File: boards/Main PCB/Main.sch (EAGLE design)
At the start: 120 parts, among them CN1 MINIB, CN2 MINIB, IC1 FT232RL, IC2 FT232RL, IC4 OKR-T_3-W12-C, J1 3_PIN_JST-XH, J2 2_PIN_JST-XH, J3 5_PIN_JST-XH, Q4 BSS138, Q5 BSS138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

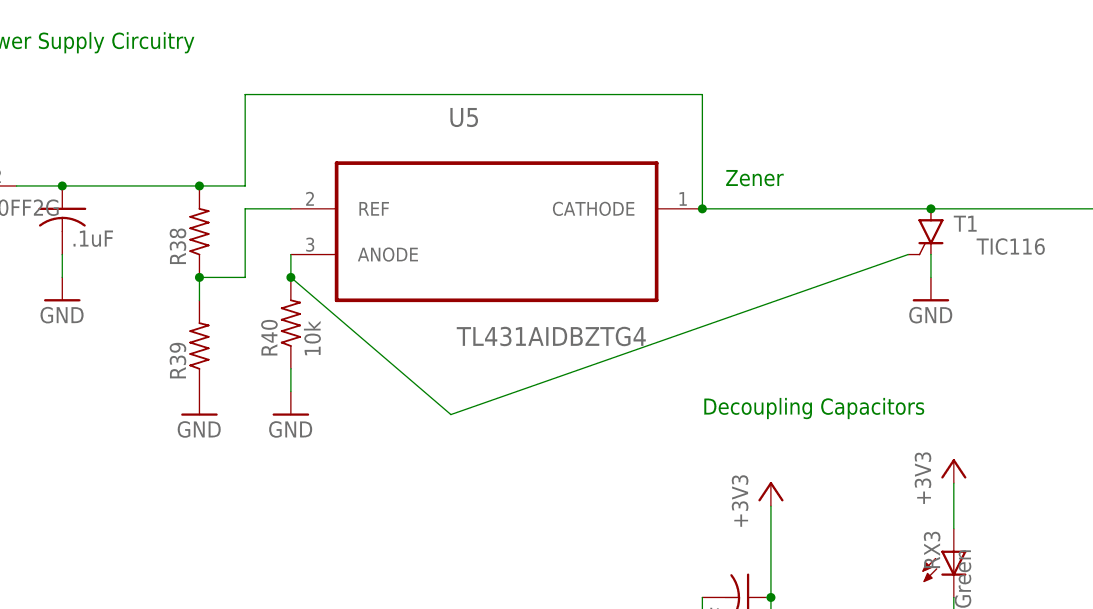
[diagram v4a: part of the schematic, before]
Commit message: Routed crowbar circuit
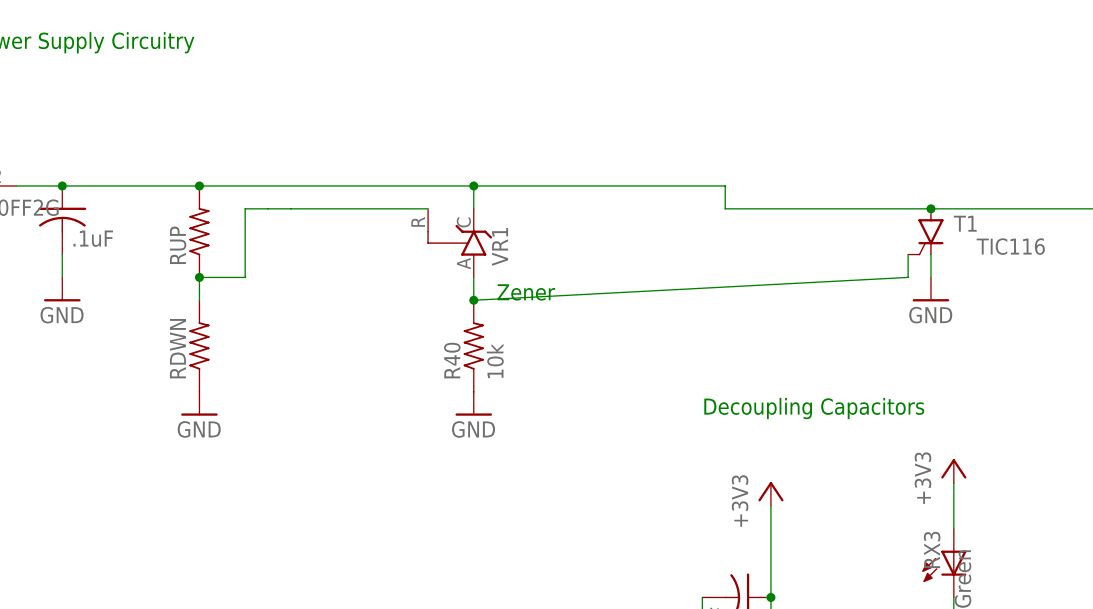
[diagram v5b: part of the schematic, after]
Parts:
- removed U5: TL431AIDBZTG4, main_library:TL431AIDBZTG4
- added VR1: (no value), v-reg:TL431CLP
- renumbered R38 to RUP, R39 to RDWN
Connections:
- removed net N$30: R40.2, T1.G, U5.ANODE
- new net N$24: R40.2, T1.G, VR1.A
- net +5V: now also VR1.C; no longer U5.CATHODE
- net N$25: now also VR1.R; no longer U5.REF
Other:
- moved on the sheet: R40
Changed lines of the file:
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@@
 <part name="C33" library="rcl" library_urn="urn:adsk.eagle:library:334" deviceset="C-US" device="C0805" package3d_urn="urn:adsk.eagle:package:23617/2" value=".1uF"/>
 <part name="GND48" library="supply1" library_urn="urn:adsk.eagle:library:371" deviceset="GND" device=""/>
-<part name="R38" library="resistor" library_urn="urn:adsk.eagle:library:348" deviceset="R-US_" device="R0805" package3d_urn="urn:adsk.eagle:package:26059/1"/>
-<part name="R39" library="resistor" library_urn="urn:adsk.eagle:library:348" deviceset="R-US_" device="R0805" package3d_urn="urn:adsk.eagle:package:26059/1"/>
+<part name="RUP" library="resistor" library_urn="urn:adsk.eagle:library:348" deviceset="R-US_" device="R0805" package3d_urn="urn:adsk.eagle:package:26059/1"/>
+<part name="RDWN" library="resistor" library_urn="urn:adsk.eagle:library:348" deviceset="R-US_" device="R0805" package3d_urn="urn:adsk.eagle:package:26059/1"/>
 <part name="GND49" library="supply1" library_urn="urn:adsk.eagle:library:371" deviceset="GND" device=""/>
-<part name="U5" library="main_library" deviceset="TL431AIDBZTG4" device=""/>
 <part name="GND50" library="supply1" library_urn="urn:adsk.eagle:library:371" deviceset="GND" device=""/>
 <part name="R40" library="resistor" library_urn="urn:adsk.eagle:library:348" deviceset="R-US_" device="R0805" package3d_urn="urn:adsk.eagle:package:26059/1" value="10k"/>
 <part name="T1" library="triac" library_urn="urn:adsk.eagle:library:403" deviceset="TIC116" device="" package3d_urn="urn:adsk.eagle:package:30140/2"/>
 <part name="GND51" library="supply1" library_urn="urn:adsk.eagle:library:371" deviceset="GND" device=""/>
+<part name="VR1" library="v-reg" library_urn="urn:adsk.eagle:library:409" deviceset="TL431CLP" device="" package3d_urn="urn:adsk.eagle:package:30363/1"/>
 </parts>
 <sheets>
@@
 <text x="122.682" y="110.744" size="1.778" layer="95">10K</text>
 <text x="112.522" y="128.524" size="1.778" layer="95">10K</text>
-<text x="406.4" y="383.54" size="1.778" layer="91">Zener</text>
+<text x="381" y="370.84" size="1.778" layer="91">Zener</text>
 </plain>
 <instances>
@@
 <attribute name="VALUE" x="474.98" y="228.6" size="1.778" layer="96"/>
 </instance>
-<instance part="R38" gate="G$1" x="347.98" y="378.46" smashed="yes" rot="R90">
+<instance part="RUP" gate="G$1" x="347.98" y="378.46" smashed="yes" rot="R90">
 <attribute name="NAME" x="346.4814" y="374.65" size="1.778" layer="95" rot="R90"/>
 <attribute name="VALUE" x="351.282" y="374.65" size="1.778" layer="96" rot="R90"/>
 </instance>
-<instance part="R39" gate="G$1" x="347.98" y="365.76" smashed="yes" rot="R90">
+<instance part="RDWN" gate="G$1" x="347.98" y="365.76" smashed="yes" rot="R90">
 <attribute name="NAME" x="346.4814" y="361.95" size="1.778" layer="95" rot="R90"/>
 <attribute name="VALUE" x="351.282" y="361.95" size="1.778" layer="96" rot="R90"/>
@@
 <attribute name="VALUE" x="345.44" y="355.6" size="1.778" layer="96"/>
 </instance>
-<instance part="U5" gate="A" x="381" y="381" smashed="yes">
-<attribute name="NAME" x="375.636409375" y="390.12573125" size="2.08443125" layer="95" ratio="10" rot="SR0"/>
-<attribute name="VALUE" x="376.57783125" y="365.7765" size="2.084009375" layer="96" ratio="10" rot="SR0"/>
-</instance>
-<instance part="GND50" gate="1" x="358.14" y="358.14" smashed="yes">
-<attribute name="VALUE" x="355.6" y="355.6" size="1.778" layer="96"/>
-</instance>
-<instance part="R40" gate="G$1" x="358.14" y="368.3" smashed="yes" rot="R90">
-<attribute name="NAME" x="356.6414" y="364.49" size="1.778" layer="95" rot="R90"/>
-<attribute name="VALUE" x="361.442" y="364.49" size="1.778" layer="96" rot="R90"/>
+<instance part="GND50" gate="1" x="378.46" y="358.14" smashed="yes">
+<attribute name="VALUE" x="375.92" y="355.6" size="1.778" layer="96"/>
+</instance>
+<instance part="R40" gate="G$1" x="378.46" y="365.76" smashed="yes" rot="R90">
+<attribute name="NAME" x="376.9614" y="361.95" size="1.778" layer="95" rot="R90"/>
+<attribute name="VALUE" x="381.762" y="361.95" size="1.778" layer="96" rot="R90"/>
 </instance>
 <instance part="T1" gate="1" x="429.26" y="378.46" smashed="yes">
@@
 <instance part="GND51" gate="1" x="429.26" y="370.84" smashed="yes">
 <attribute name="VALUE" x="426.72" y="368.3" size="1.778" layer="96"/>
+</instance>
+<instance part="VR1" gate="G$1" x="378.46" y="378.46" smashed="yes" rot="R90">
+<attribute name="NAME" x="382.27" y="374.65" size="1.778" layer="95" rot="R90"/>
+<attribute name="VALUE" x="384.175" y="374.65" size="1.778" layer="96" rot="R90"/>
 </instance>
 </instances>
@@
 </segment>
 <segment>
-<pinref part="R39" gate="G$1" pin="1"/>
+<pinref part="RDWN" gate="G$1" pin="1"/>
 <pinref part="GND49" gate="1" pin="GND"/>
-</segment>
-<segment>
-<pinref part="R40" gate="G$1" pin="1"/>
-<pinref part="GND50" gate="1" pin="GND"/>
-<wire x1="358.14" y1="363.22" x2="358.14" y2="360.68" width="0.1524" layer="91"/>
 </segment>
 <segment>
@@
 <pinref part="GND51" gate="1" pin="GND"/>
 <wire x1="429.26" y1="375.92" x2="429.26" y2="373.38" width="0.1524" layer="91"/>
+</segment>
+<segment>
+<pinref part="R40" gate="G$1" pin="1"/>
+<pinref part="GND50" gate="1" pin="GND"/>
 </segment>
 </net>
@@
 <pinref part="P+1" gate="1" pin="+5V"/>
 <wire x1="472.44" y1="388.62" x2="472.44" y2="381" width="0.1524" layer="91"/>
+<pinref part="T1" gate="1" pin="A"/>
+<wire x1="406.4" y1="381" x2="429.26" y2="381" width="0.1524" layer="91"/>
+<wire x1="429.26" y1="381" x2="472.44" y2="381" width="0.1524" layer="91"/>
+<junction x="429.26" y="381"/>
+<junction x="472.44" y="381"/>
+<pinref part="VR1" gate="G$1" pin="C"/>
+<pinref part="RUP" gate="G$1" pin="2"/>
 <pinref part="C8" gate="G$1" pin="1"/>
 <pinref part="R33" gate="G$1" pin="2"/>
 <wire x1="327.66" y1="383.54" x2="332.74" y2="383.54" width="0.1524" layer="91"/>
-<pinref part="R38" gate="G$1" pin="2"/>
+<junction x="332.74" y="383.54"/>
 <wire x1="332.74" y1="383.54" x2="347.98" y2="383.54" width="0.1524" layer="91"/>
-<junction x="332.74" y="383.54"/>
-<wire x1="347.98" y1="383.54" x2="353.06" y2="383.54" width="0.1524" layer="91"/>
-<wire x1="353.06" y1="383.54" x2="353.06" y2="393.7" width="0.1524" layer="91"/>
 <junction x="347.98" y="383.54"/>
-<pinref part="U5" gate="A" pin="CATHODE"/>
-<wire x1="353.06" y1="393.7" x2="403.86" y2="393.7" width="0.1524" layer="91"/>
-<wire x1="403.86" y1="393.7" x2="403.86" y2="381" width="0.1524" layer="91"/>
-<pinref part="T1" gate="1" pin="A"/>
-<wire x1="403.86" y1="381" x2="429.26" y2="381" width="0.1524" layer="91"/>
-<junction x="403.86" y="381"/>
-<wire x1="429.26" y1="381" x2="472.44" y2="381" width="0.1524" layer="91"/>
-<junction x="429.26" y="381"/>
-<junction x="472.44" y="381"/>
+<wire x1="347.98" y1="383.54" x2="378.46" y2="383.54" width="0.1524" layer="91"/>
+<wire x1="378.46" y1="383.54" x2="378.46" y2="381" width="0.1524" layer="91"/>
+<wire x1="378.46" y1="383.54" x2="406.4" y2="383.54" width="0.1524" layer="91"/>
+<wire x1="406.4" y1="383.54" x2="406.4" y2="381" width="0.1524" layer="91"/>
+<junction x="378.46" y="383.54"/>
 </segment>
 </net>
@@
 <net name="N$25" class="0">
 <segment>
-<pinref part="R38" gate="G$1" pin="1"/>
-<pinref part="R39" gate="G$1" pin="2"/>
+<pinref part="RUP" gate="G$1" pin="1"/>
+<pinref part="RDWN" gate="G$1" pin="2"/>
 <wire x1="347.98" y1="373.38" x2="347.98" y2="370.84" width="0.1524" layer="91"/>
 <wire x1="347.98" y1="373.38" x2="353.06" y2="373.38" width="0.1524" layer="91"/>
 <wire x1="353.06" y1="373.38" x2="353.06" y2="381" width="0.1524" layer="91"/>
 <junction x="347.98" y="373.38"/>
-<pinref part="U5" gate="A" pin="REF"/>
-<wire x1="353.06" y1="381" x2="358.14" y2="381" width="0.1524" layer="91"/>
-</segment>
-</net>
-<net name="N$30" class="0">
-<segment>
-<pinref part="U5" gate="A" pin="ANODE"/>
+<wire x1="353.06" y1="381" x2="355.6" y2="381" width="0.1524" layer="91"/>
+<pinref part="VR1" gate="G$1" pin="R"/>
+<wire x1="355.6" y1="381" x2="358.14" y2="381" width="0.1524" layer="91"/>
+<wire x1="373.38" y1="381" x2="358.14" y2="381" width="0.1524" layer="91"/>
+</segment>
+</net>
+<net name="N$24" class="0">
+<segment>
+<pinref part="VR1" gate="G$1" pin="A"/>
 <pinref part="R40" gate="G$1" pin="2"/>
-<wire x1="358.14" y1="375.92" x2="358.14" y2="373.38" width="0.1524" layer="91"/>
+<wire x1="378.46" y1="373.38" x2="378.46" y2="370.84" width="0.1524" layer="91"/>
 <pinref part="T1" gate="1" pin="G"/>
-<wire x1="358.14" y1="373.38" x2="375.92" y2="358.14" width="0.1524" layer="91"/>
-<wire x1="375.92" y1="358.14" x2="426.72" y2="375.92" width="0.1524" layer="91"/>
-<junction x="358.14" y="373.38"/>
-</segment>
-</net>
+<wire x1="378.46" y1="370.84" x2="426.72" y2="373.38" width="0.1524" layer="91"/>
+<wire x1="426.72" y1="373.38" x2="426.72" y2="375.92" width="0.1524" layer="91"/>
+<junction x="378.46" y="370.84"/>
+</segment>
+</net>

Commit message: Updating with latest PCB submission
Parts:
- removed U$3: BNO055, microbuilder:BNO055
- added U$9: (no value), main_library:MICROBUILDER_BNO055
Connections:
- net +3V3: now also U$9.NBOOT_LOAD_PIN, U$9.VDD, U$9.VDDIO; no longer U$3.NBOOT_LOAD_PIN, U$3.VDD, U$3.VDDIO
- net CAP: now also U$9.CAP; no longer U$3.CAP
- net GND: now also U$9.COM2(GND), U$9.GND@1, U$9.GND@2, U$9.PIN10(GND), U$9.PIN15(GND), U$9.PIN16(GND); no longer U$3.COM2(GND), U$3.GND@1, U$3.GND@2, U$3.PIN10(GND), U$3.PIN15(GND), U$3.PIN16(GND)
- net I2CADDR_3V: now also U$9.COM3/I2C_ADDR; no longer U$3.COM3/I2C_ADDR
- net INT_3V: now also U$9.INT; no longer U$3.INT
- net N$1: now also U$9.XIN32; no longer U$3.XIN32
- net N$10: now also U$9.XOUT32; no longer U$3.XOUT32
- net NRESET_3V: now also U$9.NRESET; no longer U$3.NRESET
- net PS0_3V: now also U$9.PS0; no longer U$3.PS0
- net PS1_3V: now also U$9.PS1; no longer U$3.PS1
- net SCL_3V: now also U$9.COM1/SCL/RX; no longer U$3.COM1/SCL/RX
- net SDA_3V: now also U$9.COM0/SDA/TX; no longer U$3.COM0/SDA/TX
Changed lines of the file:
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@@
 <?xml version="1.0" encoding="utf-8"?>
 <!DOCTYPE eagle SYSTEM "eagle.dtd">
-<eagle version="9.3.1">
+<eagle version="9.3.0">
 <drawing>
 <settings>
@@
 <part name="GND6" library="supply1" library_urn="urn:adsk.eagle:library:371" deviceset="GND" device=""/>
 <part name="R1" library="adafruit" deviceset="R-US_" device="R0805" value="10"/>
-<part name="U$3" library="microbuilder" deviceset="BNO055" device="" value="BNO055"/>
 <part name="R4" library="microbuilder" deviceset="RESISTOR" device="0805_NOOUTLINE" value="10K">
 <attribute name="10K" value=""/>
@@
 <part name="GND51" library="supply1" library_urn="urn:adsk.eagle:library:371" deviceset="GND" device=""/>
 <part name="VR1" library="v-reg" library_urn="urn:adsk.eagle:library:409" deviceset="TL431CLP" device="" package3d_urn="urn:adsk.eagle:package:30363/1"/>
+<part name="U$9" library="main_library" deviceset="MICROBUILDER_BNO055" device=""/>
 </parts>
 <sheets>
@@
 <attribute name="VALUE" x="307.34" y="353.06" size="1.778" layer="96"/>
 </instance>
-<instance part="U$3" gate="G$1" x="71.12" y="121.92" smashed="yes">
-<attribute name="VALUE" x="53.34" y="91.44" size="1.27" layer="96"/>
-</instance>
 <instance part="R4" gate="G$1" x="114.3" y="116.84" smashed="yes">
 <attribute name="VALUE" x="114.3" y="116.84" size="1.016" layer="96" font="vector" ratio="15" align="center"/>
@@
 <attribute name="NAME" x="382.27" y="374.65" size="1.778" layer="95" rot="R90"/>
 <attribute name="VALUE" x="384.175" y="374.65" size="1.778" layer="96" rot="R90"/>
+</instance>
+<instance part="U$9" gate="G$1" x="71.12" y="121.92" smashed="yes">
+<attribute name="NAME" x="53.34" y="148.59" size="1.27" layer="95"/>
+<attribute name="VALUE" x="53.34" y="91.44" size="1.27" layer="96"/>
 </instance>
 </instances>
@@
 </segment>
 <segment>
-<pinref part="U$3" gate="G$1" pin="NBOOT_LOAD_PIN"/>
 <pinref part="U$15" gate="G$1" pin="3.3V"/>
 <wire x1="91.44" y1="109.22" x2="93.98" y2="109.22" width="0.1524" layer="91"/>
-</segment>
-<segment>
-<pinref part="U$3" gate="G$1" pin="VDDIO"/>
+<pinref part="U$9" gate="G$1" pin="NBOOT_LOAD_PIN"/>
+</segment>
+<segment>
 <pinref part="U$21" gate="G$1" pin="3.3V"/>
 <wire x1="50.8" y1="137.16" x2="48.26" y2="137.16" width="0.1524" layer="91"/>
 <wire x1="48.26" y1="137.16" x2="48.26" y2="139.7" width="0.1524" layer="91"/>
-<pinref part="U$3" gate="G$1" pin="VDD"/>
 <wire x1="48.26" y1="139.7" x2="48.26" y2="142.24" width="0.1524" layer="91"/>
 <wire x1="50.8" y1="139.7" x2="48.26" y2="139.7" width="0.1524" layer="91"/>
@@
 <pinref part="C7" gate="G$1" pin="2"/>
 <wire x1="45.72" y1="139.7" x2="48.26" y2="139.7" width="0.1524" layer="91"/>
+<pinref part="U$9" gate="G$1" pin="VDD"/>
+<pinref part="U$9" gate="G$1" pin="VDDIO"/>
 </segment>
 <segment>
@@
 </segment>
 <segment>
-<pinref part="U$3" gate="G$1" pin="COM2(GND)"/>
 <pinref part="U$8" gate="G$1" pin="GND"/>
 <wire x1="124.46" y1="134.62" x2="91.44" y2="134.62" width="0.1524" layer="91"/>
+<pinref part="U$9" gate="G$1" pin="COM2(GND)"/>
 </segment>
 <segment>
@@
 </segment>
 <segment>
-<pinref part="U$3" gate="G$1" pin="PIN15(GND)"/>
 <pinref part="U$12" gate="G$1" pin="GND"/>
 <wire x1="50.8" y1="116.84" x2="48.26" y2="116.84" width="0.1524" layer="91"/>
-<pinref part="U$3" gate="G$1" pin="PIN10(GND)"/>
 <wire x1="48.26" y1="116.84" x2="45.72" y2="116.84" width="0.1524" layer="91"/>
 <wire x1="50.8" y1="119.38" x2="48.26" y2="119.38" width="0.1524" layer="91"/>
 <wire x1="48.26" y1="119.38" x2="48.26" y2="116.84" width="0.1524" layer="91"/>
 <junction x="48.26" y="116.84"/>
-<pinref part="U$3" gate="G$1" pin="PIN16(GND)"/>
 <wire x1="50.8" y1="114.3" x2="48.26" y2="114.3" width="0.1524" layer="91"/>
 <wire x1="48.26" y1="114.3" x2="48.26" y2="116.84" width="0.1524" layer="91"/>
-</segment>
-<segment>
-<pinref part="U$3" gate="G$1" pin="GND@2"/>
+<pinref part="U$9" gate="G$1" pin="PIN10(GND)"/>
+<pinref part="U$9" gate="G$1" pin="PIN15(GND)"/>
+<pinref part="U$9" gate="G$1" pin="PIN16(GND)"/>
+</segment>
+<segment>
 <pinref part="U$13" gate="G$1" pin="GND"/>
 <wire x1="50.8" y1="124.46" x2="48.26" y2="124.46" width="0.1524" layer="91"/>
-<pinref part="U$3" gate="G$1" pin="GND@1"/>
 <wire x1="48.26" y1="124.46" x2="45.72" y2="124.46" width="0.1524" layer="91"/>
 <wire x1="50.8" y1="127" x2="48.26" y2="127" width="0.1524" layer="91"/>
 <wire x1="48.26" y1="127" x2="48.26" y2="124.46" width="0.1524" layer="91"/>
 <junction x="48.26" y="124.46"/>
+<pinref part="U$9" gate="G$1" pin="GND@1"/>
+<pinref part="U$9" gate="G$1" pin="GND@2"/>
 </segment>
 <segment>
@@
 </segment>
 <segment>
-<pinref part="U$3" gate="G$1" pin="COM0/SDA/TX"/>
 <wire x1="91.44" y1="139.7" x2="104.14" y2="139.7" width="0.1524" layer="91"/>
 <label x="93.98" y="139.7" size="1.778" layer="95"/>
 <pinref part="R8" gate="G$1" pin="1"/>
+<pinref part="U$9" gate="G$1" pin="COM0/SDA/TX"/>
 </segment>
 <segment>
@@
 </segment>
 <segment>
-<pinref part="U$3" gate="G$1" pin="COM1/SCL/RX"/>
 <wire x1="91.44" y1="137.16" x2="109.22" y2="137.16" width="0.1524" layer="91"/>
 <label x="93.98" y="137.16" size="1.778" layer="95"/>
 <pinref part="R9" gate="G$1" pin="1"/>
+<pinref part="U$9" gate="G$1" pin="COM1/SCL/RX"/>
 </segment>
 <segment>
@@
 </segment>
 <segment>
-<pinref part="U$3" gate="G$1" pin="NRESET"/>
 <wire x1="91.44" y1="121.92" x2="109.22" y2="121.92" width="0.1524" layer="91"/>
 <label x="93.98" y="121.92" size="1.778" layer="95"/>
+<pinref part="U$9" gate="G$1" pin="NRESET"/>
 </segment>
 <segment>
@@
 <net name="PS1_3V" class="0">
 <segment>
-<pinref part="U$3" gate="G$1" pin="PS1"/>
 <wire x1="91.44" y1="114.3" x2="119.38" y2="114.3" width="0.1524" layer="91"/>
 <label x="93.98" y="114.3" size="1.778" layer="95"/>
 <pinref part="R6" gate="G$1" pin="1"/>
+<pinref part="U$9" gate="G$1" pin="PS1"/>
 </segment>
 <segment>
@@
 <net name="PS0_3V" class="0">
 <segment>
-<pinref part="U$3" gate="G$1" pin="PS0"/>
 <wire x1="91.44" y1="116.84" x2="109.22" y2="116.84" width="0.1524" layer="91"/>
 <label x="93.98" y="116.84" size="1.778" layer="95"/>
 <pinref part="R4" gate="G$1" pin="1"/>
+<pinref part="U$9" gate="G$1" pin="PS0"/>
 </segment>
 <segment>
@@
 <net name="INT_3V" class="0">
 <segment>
-<pinref part="U$3" gate="G$1" pin="INT"/>
 <wire x1="91.44" y1="127" x2="104.14" y2="127" width="0.1524" layer="91"/>
 <label x="93.98" y="127" size="1.778" layer="95"/>
+<pinref part="U$9" gate="G$1" pin="INT"/>
 </segment>
 <segment>
@@
 <net name="I2CADDR_3V" class="0">
 <segment>
-<pinref part="U$3" gate="G$1" pin="COM3/I2C_ADDR"/>
 <pinref part="R7" gate="G$1" pin="1"/>
 <wire x1="91.44" y1="132.08" x2="109.22" y2="132.08" width="0.1524" layer="91"/>
 <label x="93.98" y="132.08" size="1.778" layer="95"/>
+<pinref part="U$9" gate="G$1" pin="COM3/I2C_ADDR"/>
 </segment>
 <segment>
@@
 <net name="N$1" class="0">
 <segment>
-<pinref part="U$3" gate="G$1" pin="XIN32"/>
 <pinref part="C4" gate="G$1" pin="2"/>
 <wire x1="50.8" y1="109.22" x2="38.1" y2="109.22" width="0.1524" layer="91"/>
@@
 <wire x1="38.1" y1="104.14" x2="38.1" y2="109.22" width="0.1524" layer="91"/>
 <junction x="38.1" y="109.22"/>
+<pinref part="U$9" gate="G$1" pin="XIN32"/>
 </segment>
 </net>
 <net name="N$10" class="0">
 <segment>
-<pinref part="U$3" gate="G$1" pin="XOUT32"/>
 <wire x1="50.8" y1="104.14" x2="43.18" y2="104.14" width="0.1524" layer="91"/>
 <wire x1="43.18" y1="104.14" x2="43.18" y2="93.98" width="0.1524" layer="91"/>
@@
 <wire x1="38.1" y1="99.06" x2="38.1" y2="93.98" width="0.1524" layer="91"/>
 <junction x="38.1" y="93.98"/>
+<pinref part="U$9" gate="G$1" pin="XOUT32"/>
 </segment>
 </net>
 <net name="CAP" class="0">
 <segment>
-<pinref part="U$3" gate="G$1" pin="CAP"/>
 <pinref part="C6" gate="G$1" pin="2"/>
 <wire x1="50.8" y1="132.08" x2="45.72" y2="132.08" width="0.1524" layer="91"/>
-</segment>
-</net>
+<pinref part="U$9" gate="G$1" pin="CAP"/>
+</segment>
+</net>
